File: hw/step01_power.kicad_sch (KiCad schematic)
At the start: 11 parts, among them J1 USB_C_Receptacle_PowerOnly_6P, U1 MCP1727-0802xMF

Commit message: test: introduce ERC violation
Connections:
- net GND: no longer U1.4 (GND), U1.9 (GND)
- new net: U1.4 (GND), U1.9 (GND)
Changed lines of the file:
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@@
-	)
-	(junction
-		(at 184.15 133.35)
-		(diameter 0)
-		(color 0 0 0 0)
 	)
 	(junction
@@
 	(wire
 		(pts
-			(xy 184.15 133.35) (xy 204.47 133.35)
+			(xy 158.75 133.35) (xy 204.47 133.35)
 		)
 		(stroke
@@
 	(wire
 		(pts
-			(xy 184.15 86.36) (xy 184.15 133.35)
-		)
-		(stroke
-			(width 0)
-			(type default)
-		)
-	)
-	(wire
-		(pts
 			(xy 204.47 76.2) (xy 204.47 97.79)
 		)
@@
 		)
 		(stroke
-			(width 0)
-			(type default)
-		)
-	)
-	(wire
-		(pts
-			(xy 158.75 133.35) (xy 184.15 133.35)
-		)
-		(stroke

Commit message: fix(hw): resolve ERC violations in step01_power
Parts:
- renumbered C_IN to C_IN1, C_IN to C_IN2, C_OUT to C_OUT1, C_OUT to C_OUT2
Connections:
- net GND: now also U1.4 (GND), U1.9 (GND)
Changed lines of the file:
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@@
+	)
+	(junction
+		(at 184.15 133.35)
+		(diameter 0)
+		(color 0 0 0 0)
 	)
 	(junction
@@
 	(wire
 		(pts
+			(xy 184.15 133.35) (xy 204.47 133.35)
+		)
+		(stroke
+			(width 0)
+			(type default)
+		)
+	)
+	(wire
+		(pts
 			(xy 204.47 133.35) (xy 219.71 133.35)
 		)
@@
 	(wire
 		(pts
-			(xy 158.75 133.35) (xy 204.47 133.35)
+			(xy 158.75 133.35) (xy 184.15 133.35)
 		)
 		(stroke
@@
 		(pts
 			(xy 219.71 105.41) (xy 219.71 133.35)
+		)
+		(stroke
+			(width 0)
+			(type default)
+		)
+	)
+	(wire
+		(pts
+			(xy 184.15 86.36) (xy 184.15 133.35)
 		)
 		(stroke
@@
 		(dnp no)
 		(fields_autoplaced yes)
-		(property "Reference" "C_OUT"
+		(property "Reference" "C_OUT1"
 			(at 208.28 100.3299 0)
 			(effects
@@
 			(project ""
 				(path "/7b66d93d-d6d0-4bd4-83b3-6fc711e21073"
-					(reference "C_OUT")
+					(reference "C_OUT1")
 					(unit 1)
 				)
@@
 		(dnp no)
 		(fields_autoplaced yes)
-		(property "Reference" "C_OUT"
+		(property "Reference" "C_OUT2"
 			(at 223.52 100.3299 0)
 			(effects
@@
 			(project ""
 				(path "/7b66d93d-d6d0-4bd4-83b3-6fc711e21073"
-					(reference "C_OUT")
+					(reference "C_OUT2")
 					(unit 1)
 				)
@@
 		(dnp no)
 		(fields_autoplaced yes)
-		(property "Reference" "C_IN"
+		(property "Reference" "C_IN1"
 			(at 152.4 97.7899 0)
 			(effects
@@
 			(project ""
 				(path "/7b66d93d-d6d0-4bd4-83b3-6fc711e21073"
-					(reference "C_IN")
+					(reference "C_IN1")
 					(unit 1)
 				)
@@
 		(dnp no)
 		(fields_autoplaced yes)
-		(property "Reference" "C_IN"
+		(property "Reference" "C_IN2"
 			(at 162.56 97.7899 0)
 			(effects
@@
 			(project ""
 				(path "/7b66d93d-d6d0-4bd4-83b3-6fc711e21073"
-					(reference "C_IN")
+					(reference "C_IN2")
 					(unit 1)
 				)

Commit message: docs: clarify PCB power bring-up; unify power net labels
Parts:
- removed U1: MCP1727-0802xMF, Package_DFN_QFN:DFN-8-1EP_3x3mm_P0.65mm_EP1.55x2.4mm, symbol Regulator_Linear:MCP1727-0802xMF
- added TP1: TP_VBUS, symbol Connector:TestPoint
- added TP2: TP_GND, symbol Connector:TestPoint
- added TP4: TP_VBUS_PRO, symbol Connector:TestPoint
- added U2: MCP1727-3302xMF, Package_DFN_QFN:DFN-8-1EP_3x3mm_P0.65mm_EP1.55x2.4mm, symbol Regulator_Linear:MCP1727-3302xMF
- TP3: renamed from TP1; value TestPoint -> TP_3V3
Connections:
- net GND: now also TP2.1, U2.4 (GND), U2.9 (GND)
- net VBUS_IN: now also TP1.1
- net 3V3 renamed +3V3
- net +3V3: now also U2.7 (Sense), U2.8 (Vout)
- net VBUS_PROT renamed VBUS_PRO
- net VBUS_PRO: now also TP4.1, U2.1 (Vin), U2.2 (Vin), U2.3 (~{SHDN})

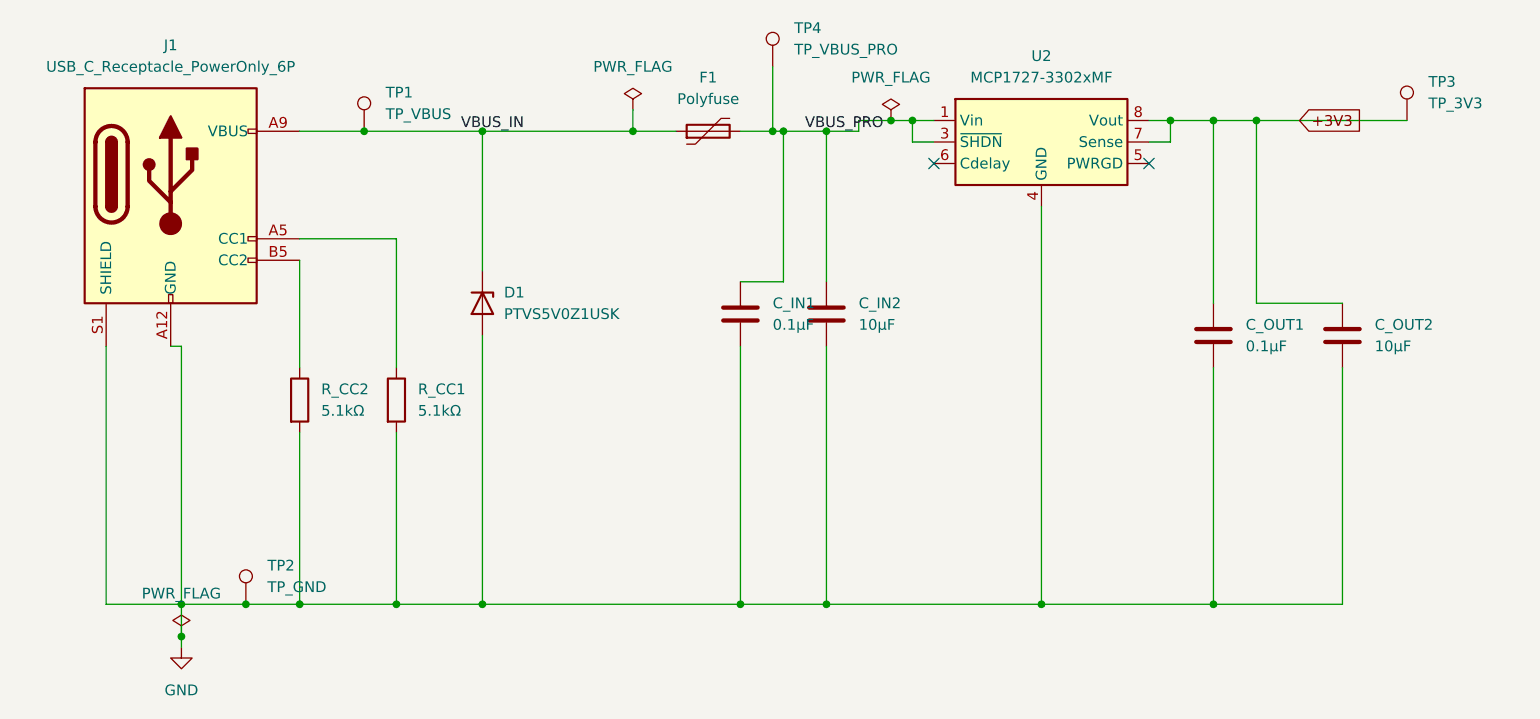
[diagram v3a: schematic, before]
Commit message: Issue #25: add Polyfuse_TBD project symbol and schematic updates
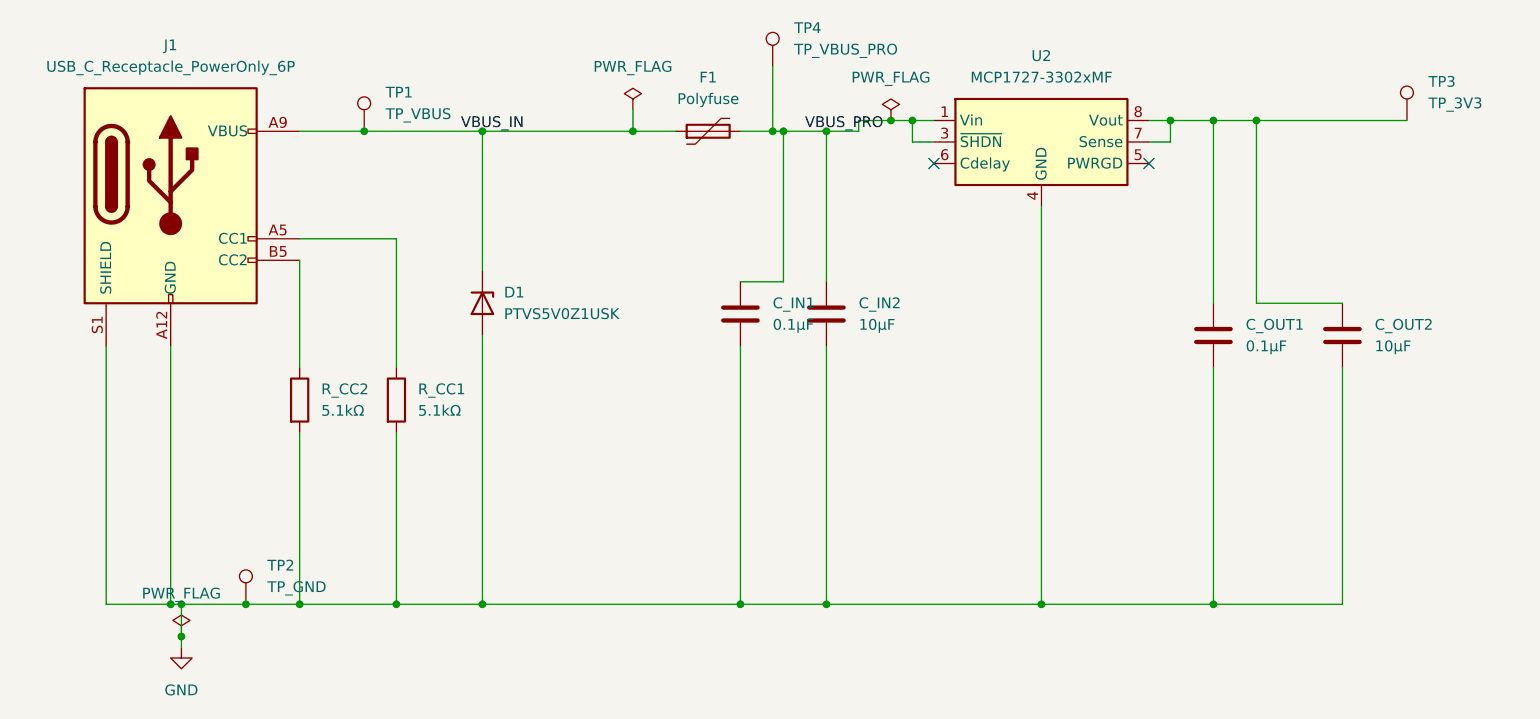
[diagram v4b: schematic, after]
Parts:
- C_IN1, C_IN2, C_OUT1, C_OUT2: footprint (none) -> Capacitor_SMD:C_0603_1608Metric
- F1: footprint (none) -> Fuse:Fuse_1812_4532Metric; symbol Device:Polyfuse -> hw_symbols:Polyfuse_TBD
- J1: footprint (none) -> Connector_USB:USB_C_Receptacle_HRO_TYPE-C-31-M-12
- R_CC1, R_CC2: footprint (none) -> Resistor_SMD:R_0603_1608Metric
- TP1, TP2, TP3, TP4: footprint (none) -> TestPoint:TestPoint_Pad_D1.0mm
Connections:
- net +3V3: no longer names the net of C_OUT1.1, C_OUT2.1, TP3.1, U2.7 (Sense), U2.8 (Vout)
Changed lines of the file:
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@@
+	)
+	(junction
+		(at 81.28 133.35)
+		(diameter 0)
+		(color 0 0 0 0)
 	)
 	(junction
@@
 	(wire
 		(pts
-			(xy 73.66 133.35) (xy 82.55 133.35)
+			(xy 73.66 133.35) (xy 81.28 133.35)
 		)
 		(stroke
@@
 	(wire
 		(pts
+			(xy 81.28 102.87) (xy 81.28 133.35)
+		)
+		(stroke
+			(width 0)
+			(type default)
+		)
+	)
+	(wire
+		(pts
 			(xy 107.95 113.03) (xy 107.95 133.35)
 		)
@@
 	(wire
 		(pts
+			(xy 81.28 133.35) (xy 82.55 133.35)
+		)
+		(stroke
+			(width 0)
+			(type default)
+		)
+	)
+	(wire
+		(pts
 			(xy 158.75 133.35) (xy 184.15 133.35)
 		)
@@
 	(wire
 		(pts
-			(xy 82.55 102.87) (xy 82.55 133.35)
-		)
-		(stroke
-			(width 0)
-			(type default)
-		)
-	)
-	(wire
-		(pts
 			(xy 135.89 74.93) (xy 135.89 77.47)
 		)
@@
 		(pts
 			(xy 107.95 133.35) (xy 118.11 133.35)
-		)
-		(stroke
-			(width 0)
-			(type default)
-		)
-	)
-	(wire
-		(pts
-			(xy 82.55 102.87) (xy 81.28 102.87)
 		)
 		(stroke
@@
 			)
 			(justify left bottom)
-		)
-	)
-	(global_label "+3V3"
-		(shape input)
-		(at 214.63 76.2 0)
-		(fields_autoplaced yes)
-		(effects
-			(font
-				(size 1.27 1.27)
-			)
-			(justify left)
-		)
-		(property "Intersheetrefs" "${INTERSHEET_REFS}"
-			(at 221.1228 76.2 0)
-			(effects
-				(font
-					(size 1.27 1.27)
-				)
-				(justify left)
-				(hide yes)
-			)
 		)
 	)
@@
 					(unit 1)
 				)
+				(path "/7b66d93d-d6d0-4bd4-83b3-6fc711e21073/d394618b-0e7e-457f-a476-ce5e8d3d9e88"
+					(reference "U2")
+					(unit 1)
+				)
 			)
 		)
@@
 					(unit 1)
 				)
+				(path "/7b66d93d-d6d0-4bd4-83b3-6fc711e21073/d394618b-0e7e-457f-a476-ce5e8d3d9e88"
+					(reference "#FLG01")
+					(unit 1)
+				)
 			)
 		)
@@
 					(unit 1)
 				)
+				(path "/7b66d93d-d6d0-4bd4-83b3-6fc711e21073/d394618b-0e7e-457f-a476-ce5e8d3d9e88"
+					(reference "D1")
+					(unit 1)
+				)
 			)
 		)
@@
 			)
 		)
-		(property "Footprint" ""
+		(property "Footprint" "Resistor_SMD:R_0603_1608Metric"
 			(at 94.742 109.22 90)
 			(effects
@@
 			(project ""
 				(path "/7b66d93d-d6d0-4bd4-83b3-6fc711e21073"
+					(reference "R_CC2")
+					(unit 1)
+				)
+				(path "/7b66d93d-d6d0-4bd4-83b3-6fc711e21073/d394618b-0e7e-457f-a476-ce5e8d3d9e88"
 					(reference "R_CC2")
 					(unit 1)
@@
 			)
 		)
-		(property "Footprint" ""
+		(property "Footprint" "TestPoint:TestPoint_Pad_D1.0mm"
 			(at 157.48 69.85 0)
 			(effects
@@
 			(project ""
 				(path "/7b66d93d-d6d0-4bd4-83b3-6fc711e21073"
+					(reference "TP4")
+					(unit 1)
+				)
+				(path "/7b66d93d-d6d0-4bd4-83b3-6fc711e21073/d394618b-0e7e-457f-a476-ce5e8d3d9e88"
 					(reference "TP4")
 					(unit 1)
@@
 			)
 		)
-		(property "Footprint" ""
+		(property "Footprint" "Connector_USB:USB_C_Receptacle_HRO_TYPE-C-31-M-12"
 			(at 85.09 82.55 0)
 			(effects
@@
 			(project ""
 				(path "/7b66d93d-d6d0-4bd4-83b3-6fc711e21073"
+					(reference "J1")
+					(unit 1)
+				)
+				(path "/7b66d93d-d6d0-4bd4-83b3-6fc711e21073/d394618b-0e7e-457f-a476-ce5e8d3d9e88"
 					(reference "J1")
 					(unit 1)
@@
 			)
 		)
-		(property "Footprint" ""
+		(property "Footprint" "Capacitor_SMD:C_0603_1608Metric"
 			(at 205.4352 105.41 0)
 			(effects
@@
 			(project ""
 				(path "/7b66d93d-d6d0-4bd4-83b3-6fc711e21073"
+					(reference "C_OUT1")
+					(unit 1)
+				)
+				(path "/7b66d93d-d6d0-4bd4-83b3-6fc711e21073/d394618b-0e7e-457f-a476-ce5e8d3d9e88"
 					(reference "C_OUT1")
 					(unit 1)
@@
 					(unit 1)
 				)
+				(path "/7b66d93d-d6d0-4bd4-83b3-6fc711e21073/d394618b-0e7e-457f-a476-ce5e8d3d9e88"
+					(reference "#FLG03")
+					(unit 1)
+				)
 			)
 		)
@@
 					(unit 1)
 				)
+				(path "/7b66d93d-d6d0-4bd4-83b3-6fc711e21073/d394618b-0e7e-457f-a476-ce5e8d3d9e88"
+					(reference "#PWR01")
+					(unit 1)
+				)
 			)
 		)
 	)
 	(symbol
-		(lib_id "Device:Polyfuse")
+		(lib_id "hw_symbols:Polyfuse_TBD")
 		(at 144.78 77.47 90)
 		(unit 1)
@@
 			)
 		)
-		(property "Footprint" ""
+		(property "Footprint" "Fuse:Fuse_1812_4532Metric"
 			(at 149.86 76.2 0)
 			(effects
@@
 			(project ""
 				(path "/7b66d93d-d6d0-4bd4-83b3-6fc711e21073"
+					(reference "F1")
+					(unit 1)
+				)
+				(path "/7b66d93d-d6d0-4bd4-83b3-6fc711e21073/d394618b-0e7e-457f-a476-ce5e8d3d9e88"
 					(reference "F1")
 					(unit 1)
@@
 			)
 		)
-		(property "Footprint" ""
+		(property "Footprint" "Resistor_SMD:R_0603_1608Metric"
 			(at 106.172 109.22 90)
 			(effects
@@
 			(project ""
 				(path "/7b66d93d-d6d0-4bd4-83b3-6fc711e21073"
+					(reference "R_CC1")
+					(unit 1)
+				)
+				(path "/7b66d93d-d6d0-4bd4-83b3-6fc711e21073/d394618b-0e7e-457f-a476-ce5e8d3d9e88"
 					(reference "R_CC1")
 					(unit 1)
@@
 					(unit 1)
 				)
+				(path "/7b66d93d-d6d0-4bd4-83b3-6fc711e21073/d394618b-0e7e-457f-a476-ce5e8d3d9e88"
+					(reference "#FLG02")
+					(unit 1)
+				)
 			)
 		)
@@
 			)
 		)
-		(property "Footprint" ""
+		(property "Footprint" "Capacitor_SMD:C_0603_1608Metric"
 			(at 220.6752 105.41 0)
 			(effects
@@
 			(project ""
 				(path "/7b66d93d-d6d0-4bd4-83b3-6fc711e21073"
+					(reference "C_OUT2")
+					(unit 1)
+				)
+				(path "/7b66d93d-d6d0-4bd4-83b3-6fc711e21073/d394618b-0e7e-457f-a476-ce5e8d3d9e88"
 					(reference "C_OUT2")
 					(unit 1)
@@
 			)
 		)
-		(property "Footprint" ""
+		(property "Footprint" "Capacitor_SMD:C_0603_1608Metric"
 			(at 149.5552 102.87 0)
 			(effects
@@
 			(project ""
 				(path "/7b66d93d-d6d0-4bd4-83b3-6fc711e21073"
+					(reference "C_IN1")
+					(unit 1)
+				)
+				(path "/7b66d93d-d6d0-4bd4-83b3-6fc711e21073/d394618b-0e7e-457f-a476-ce5e8d3d9e88"
 					(reference "C_IN1")
 					(unit 1)
@@
 			)
 		)
-		(property "Footprint" ""
+		(property "Footprint" "TestPoint:TestPoint_Pad_D1.0mm"
 			(at 95.25 133.35 0)
 			(effects
@@
 			(project ""
 				(path "/7b66d93d-d6d0-4bd4-83b3-6fc711e21073"
+					(reference "TP2")
+					(unit 1)
+				)
+				(path "/7b66d93d-d6d0-4bd4-83b3-6fc711e21073/d394618b-0e7e-457f-a476-ce5e8d3d9e88"
 					(reference "TP2")
 					(unit 1)
@@
 			)
 		)
-		(property "Footprint" ""
+		(property "Footprint" "TestPoint:TestPoint_Pad_D1.0mm"
 			(at 232.41 76.2 0)
 			(effects
@@
 			(project ""
 				(path "/7b66d93d-d6d0-4bd4-83b3-6fc711e21073"
+					(reference "TP3")
+					(unit 1)
+				)
+				(path "/7b66d93d-d6d0-4bd4-83b3-6fc711e21073/d394618b-0e7e-457f-a476-ce5e8d3d9e88"
 					(reference "TP3")
 					(unit 1)
@@
 			)
 		)
-		(property "Footprint" ""
+		(property "Footprint" "Capacitor_SMD:C_0603_1608Metric"
 			(at 159.7152 102.87 0)
 			(effects
@@
 			(project ""
 				(path "/7b66d93d-d6d0-4bd4-83b3-6fc711e21073"
+					(reference "C_IN2")
+					(unit 1)
+				)
+				(path "/7b66d93d-d6d0-4bd4-83b3-6fc711e21073/d394618b-0e7e-457f-a476-ce5e8d3d9e88"
 					(reference "C_IN2")
 					(unit 1)
@@
 			)
 		)
-		(property "Footprint" ""
+		(property "Footprint" "TestPoint:TestPoint_Pad_D1.0mm"
 			(at 109.22 77.47 0)
 			(effects
@@
 					(unit 1)
 				)
-			)
-		)
-	)
-	(sheet_instances
-		(path "/"
-			(page "1")
-		)
-	)
-	(embedded_fonts no)
+				(path "/7b66d93d-d6d0-4bd4-83b3-6fc711e21073/d394618b-0e7e-457f-a476-ce5e8d3d9e88"
+					(reference "TP1")
+					(unit 1)
+				)
+			)
+		)
+	)
 )
